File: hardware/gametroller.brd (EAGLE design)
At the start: 45.7 x 31.8 mm, 51 parts, among them J1 microUSB, J2 PJ-002AH-SMT-TR, J3 USB-A, SW1 SPST_TACT-KMR2, U1 LP5907MFX-3.3/NOPB, U16 AOZ1280CI, U2 TPS2115AIPWRQ1-SON8, U4 ATSAMD21G18_QFN, X2 32.768

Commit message: Minor modifications and cleanup to PCB
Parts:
- added F1: 500mA, gametroller:R0603
- turned C18 to 90 degrees
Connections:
- new net N$4: F1.1, J1.1
- net D+: now also J3.3; no longer J3.2
- net D-: now also J3.2; no longer J3.3
- net VBUS: now also F1.2; no longer J1.1
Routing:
- net VBUS: track 37.8 -> 41.3 mm
- net N$4: track 0.00 -> 2.48 mm
- net GND: track 62.3 -> 61.9 mm, vias 45 -> 54
- added copper zone on layer 16, net USB-SHIELD
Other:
- board text added: "3.3V 48MHz"
- board text removed: "3.3V - 48MHz"
- board text removed: "WB <3 NS"

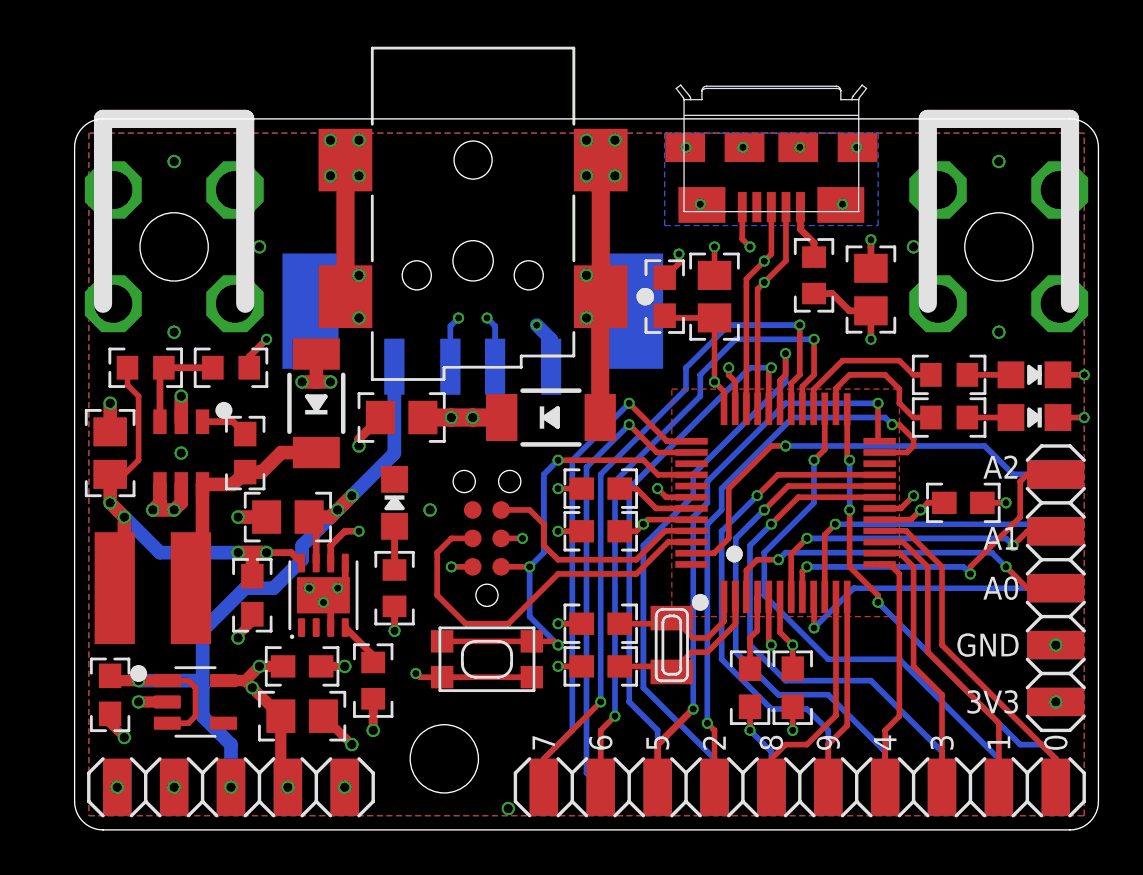
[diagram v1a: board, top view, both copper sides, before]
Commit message: Added 22M pullup resistors to several IO pins to allow board to be used as a MaKeyMaKey clone
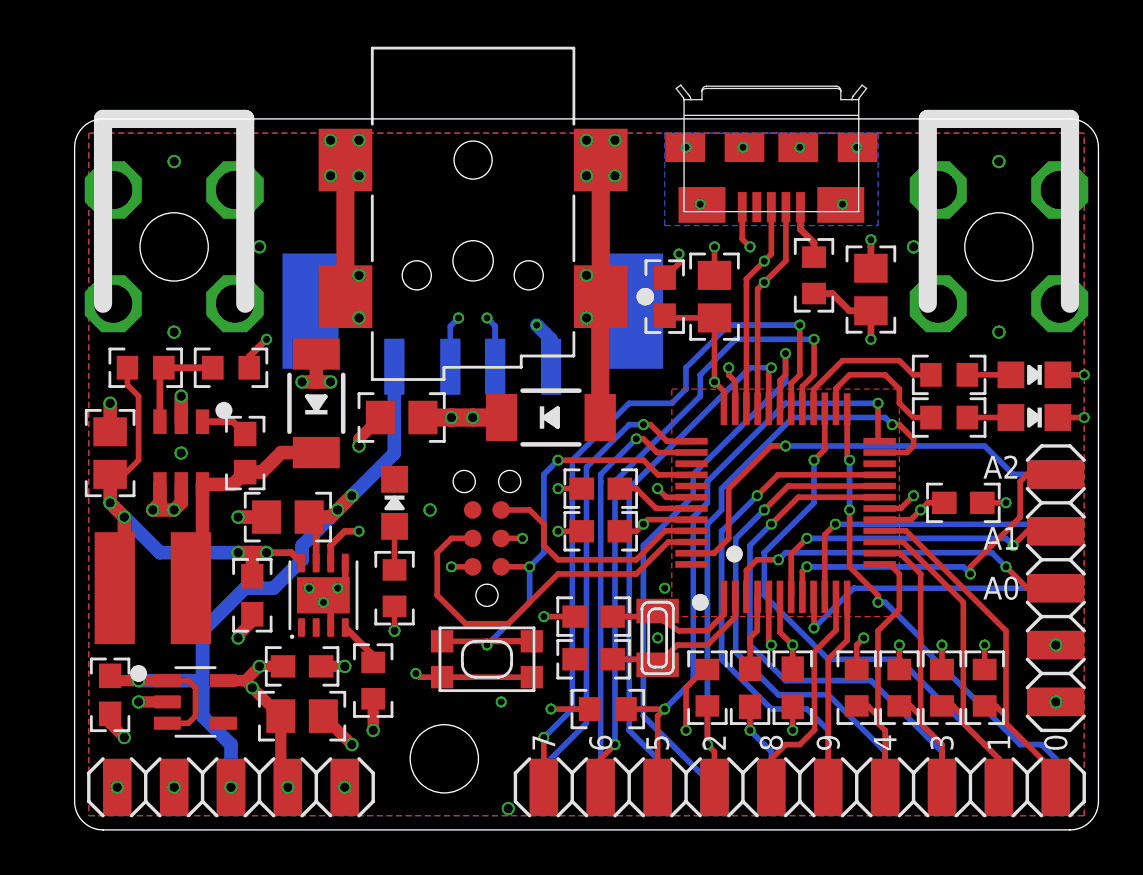
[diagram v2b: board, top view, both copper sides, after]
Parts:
- added R10, R11, R12, R4, R8, R9: 22M, gametroller:R0603
- moved X2 0.71 mm to (26.0, 8.57)
- moved C2 0.45 mm to (23.2, 9.53)
- moved C4 0.45 mm to (23.2, 7.62)
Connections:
- net +3V3: now also R10.1, R11.1, R12.1, R4.1, R8.1, R9.1
- net D0: now also R4.2
- net D1: now also R8.2
- net D2: now also R11.2
- net D3: now also R9.2
- net D4: now also R10.2
- net D5: now also R12.2
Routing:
- net +3V3: track 27.1 -> 36.8 mm, vias 10 -> 16
- net D2: track 26.0 -> 27.9 mm
- net D5: track 25.4 -> 27.1 mm
- net RXD: track 20.5 -> 18.9 mm
- net D4: track 10.8 -> 12.2 mm
- net TXD: track 22.2 -> 20.9 mm
- net D1: track 13.8 -> 14.9 mm
- net D3: track 12.1 -> 13.3 mm
- net D0: track 15.4 -> 16.5 mm
- net D7: track 31.1 -> 32.2 mm
- net !RESET: track 22.1 -> 23.1 mm
- net GND: track 61.9 -> 61.1 mm, vias 54 -> 56

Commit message: Updated BOM attributes for currently available parts
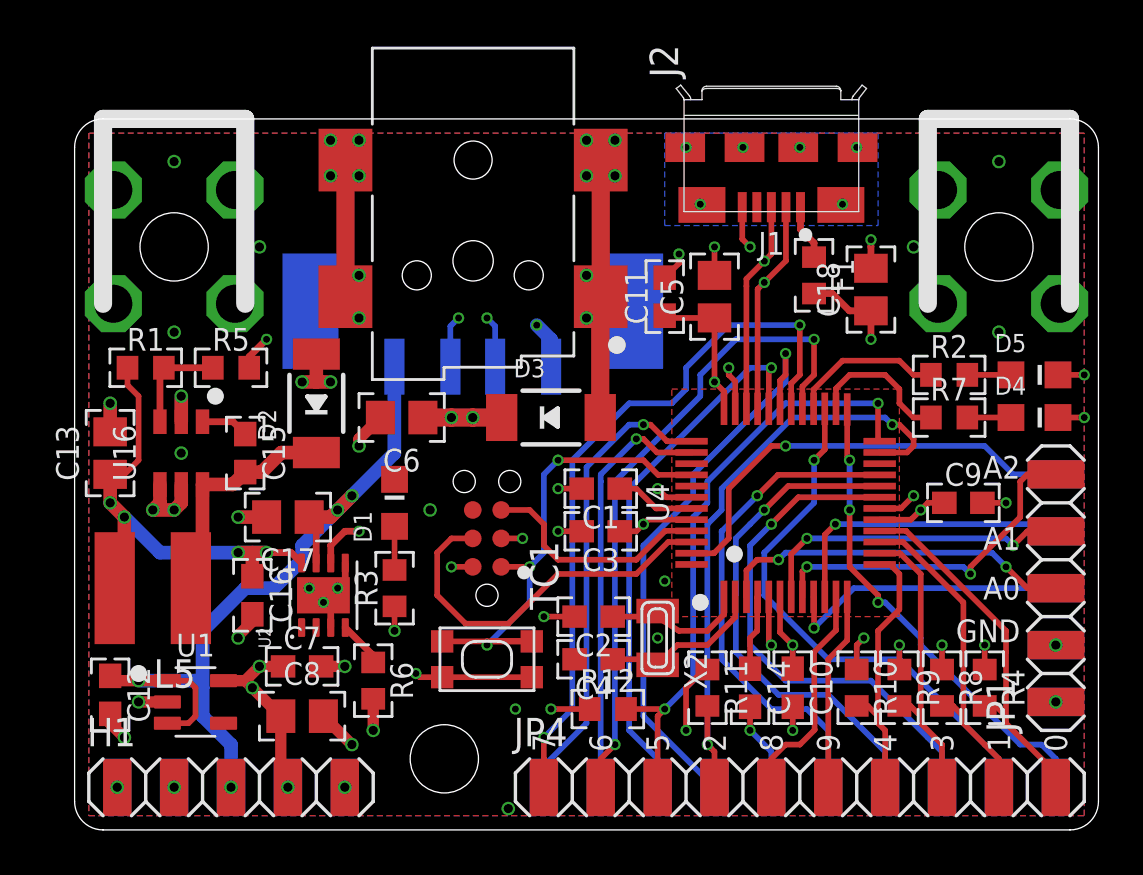
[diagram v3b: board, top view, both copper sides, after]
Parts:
- C13, C17, C6, C8: value 10µF -> 10uF
- D2, D3: value (none) -> 30V, 2A
- J1: value microUSB -> USB-MICRO
- U4: value ATSAMD21G18_QFN -> ATSAMD21G18
